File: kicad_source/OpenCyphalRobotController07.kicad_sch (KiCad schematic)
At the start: 23 parts, among them J1 SM04B-SRSS-TB, J2 RASPBERRYPI_PICO, J3 SM04B-SRSS-TB, J4 S3B-PH-SM4-TB, SW1 PTS636 SM43 SMTR LFS, U1 24LC64-I/SN

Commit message: made first draft of layout
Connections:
- net INH12: now also J2.15 (GP11/SPI1_TX/I2C1_SCL); no longer J2.14 (GP10/SPI1_SCK/I2C1_SDA)
- net INH34: now also J2.14 (GP10/SPI1_SCK/I2C1_SDA); no longer J2.15 (GP11/SPI1_TX/I2C1_SCL)
- net PWM1: now also J2.12 (GP9/SPI1_CS/I2C0_SCL/UART1_RX); no longer J2.9 (GP6/SPI0_SCK/I2C1_SDA)
- net PWM2: now also J2.11 (GP8/SPI1_RX/I2C0_SDA/UART1_TX); no longer J2.10 (GP7/SPI0_TX/I2C1_SCL)
- net PWM3: now also J2.10 (GP7/SPI0_TX/I2C1_SCL); no longer J2.11 (GP8/SPI1_RX/I2C0_SDA/UART1_TX)
- net PWM4: now also J2.9 (GP6/SPI0_SCK/I2C1_SDA); no longer J2.12 (GP9/SPI1_CS/I2C0_SCL/UART1_RX)
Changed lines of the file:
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@@
     (effects (font (size 1.27 1.27)) (justify right bottom))
   )
-  (label "PWM3" (at 53.34 57.15 180)
+  (label "PWM3" (at 53.34 54.61 180)
     (effects (font (size 1.27 1.27)) (justify right bottom))
   )
-  (label "PWM1" (at 53.34 52.07 180)
+  (label "PWM1" (at 53.34 59.69 180)
     (effects (font (size 1.27 1.27)) (justify right bottom))
   )
@@
     (effects (font (size 1.27 1.27)) (justify right bottom))
   )
-  (label "INH34" (at 53.34 67.31 180)
+  (label "INH34" (at 53.34 64.77 180)
     (effects (font (size 1.27 1.27)) (justify right bottom))
   )
@@
     (effects (font (size 1.27 1.27)) (justify left bottom))
   )
-  (label "INH12" (at 53.34 64.77 180)
+  (label "INH12" (at 53.34 67.31 180)
     (effects (font (size 1.27 1.27)) (justify right bottom))
   )
-  (label "PWM2" (at 53.34 54.61 180)
+  (label "PWM2" (at 53.34 57.15 180)
     (effects (font (size 1.27 1.27)) (justify right bottom))
   )
@@
     (effects (font (size 1.27 1.27)) (justify left bottom))
   )
-  (label "PWM4" (at 53.34 59.69 180)
+  (label "PWM4" (at 53.34 52.07 180)
     (effects (font (size 1.27 1.27)) (justify right bottom))
   )
@@
     (effects (font (size 1.27 1.27)) (justify right bottom))
   )
-  (global_label "PWM1" (shape output) (at 40.64 52.07 180) (fields_autoplaced)
+  (global_label "PWM1" (shape output) (at 40.64 59.69 180) (fields_autoplaced)
     (effects (font (size 1.27 1.27)) (justify right))
-    (property "Referenzen zwischen Schaltplänen" "${INTERSHEET_REFS}" (id 0) (at 32.9334 51.9906 0)
+    (property "Referenzen zwischen Schaltplänen" "${INTERSHEET_REFS}" (id 0) (at 32.9334 59.6106 0)
       (effects (font (size 1.27 1.27)) (justify right) hide)
     )
@@
     )
   )
-  (global_label "PWM2" (shape output) (at 40.64 54.61 180) (fields_autoplaced)
+  (global_label "PWM2" (shape output) (at 40.64 57.15 180) (fields_autoplaced)
+    (effects (font (size 1.27 1.27)) (justify right))
+    (property "Referenzen zwischen Schaltplänen" "${INTERSHEET_REFS}" (id 0) (at 32.9334 57.0706 0)
+      (effects (font (size 1.27 1.27)) (justify right) hide)
+    )
+  )
+  (global_label "PWM3" (shape output) (at 40.64 54.61 180) (fields_autoplaced)
     (effects (font (size 1.27 1.27)) (justify right))
     (property "Referenzen zwischen Schaltplänen" "${INTERSHEET_REFS}" (id 0) (at 32.9334 54.5306 0)
@@
     )
   )
-  (global_label "PWM3" (shape output) (at 40.64 57.15 180) (fields_autoplaced)
+  (global_label "INH12" (shape output) (at 40.64 67.31 180) (fields_autoplaced)
     (effects (font (size 1.27 1.27)) (justify right))
-    (property "Referenzen zwischen Schaltplänen" "${INTERSHEET_REFS}" (id 0) (at 32.9334 57.0706 0)
-      (effects (font (size 1.27 1.27)) (justify right) hide)
-    )
-  )
-  (global_label "INH12" (shape output) (at 40.64 64.77 180) (fields_autoplaced)
-    (effects (font (size 1.27 1.27)) (justify right))
-    (property "Referenzen zwischen Schaltplänen" "${INTERSHEET_REFS}" (id 0) (at 32.631 64.6906 0)
+    (property "Referenzen zwischen Schaltplänen" "${INTERSHEET_REFS}" (id 0) (at 32.631 67.2306 0)
       (effects (font (size 1.27 1.27)) (justify right) hide)
     )
@@
     )
   )
-  (global_label "INH34" (shape output) (at 40.64 67.31 180) (fields_autoplaced)
+  (global_label "INH34" (shape output) (at 40.64 64.77 180) (fields_autoplaced)
     (effects (font (size 1.27 1.27)) (justify right))
-    (property "Referenzen zwischen Schaltplänen" "${INTERSHEET_REFS}" (id 0) (at 32.631 67.2306 0)
+    (property "Referenzen zwischen Schaltplänen" "${INTERSHEET_REFS}" (id 0) (at 32.631 64.6906 0)
       (effects (font (size 1.27 1.27)) (justify right) hide)
     )
   )
-  (global_label "PWM4" (shape output) (at 40.64 59.69 180) (fields_autoplaced)
+  (global_label "PWM4" (shape output) (at 40.64 52.07 180) (fields_autoplaced)
     (effects (font (size 1.27 1.27)) (justify right))
-    (property "Referenzen zwischen Schaltplänen" "${INTERSHEET_REFS}" (id 0) (at 32.9334 59.6106 0)
+    (property "Referenzen zwischen Schaltplänen" "${INTERSHEET_REFS}" (id 0) (at 32.9334 51.9906 0)
       (effects (font (size 1.27 1.27)) (justify right) hide)
     )
@@
     )
     (path "/00000000-0000-0000-0000-00005ed92f9c/00000000-0000-0000-0000-000062500ca8"
-      (reference "J5") (unit 1) (value "SM04B-GHS-TB") (footprint "Connector_JST:JST_GH_SM04B-GHS-TB_1x04-1MP_P1.25mm_Horizontal")
+      (reference "J5") (unit 1) (value "BM04B-GHS-TBT") (footprint "Connector_JST:JST_GH_BM04B-GHS-TBT_1x04-1MP_P1.25mm_Vertical")
     )
     (path "/00000000-0000-0000-0000-00005ed92f9c/00000000-0000-0000-0000-000062500cbc"
-      (reference "J6") (unit 1) (value "SM04B-GHS-TB") (footprint "Connector_JST:JST_GH_SM04B-GHS-TB_1x04-1MP_P1.25mm_Horizontal")
+      (reference "J6") (unit 1) (value "BM04B-GHS-TBT") (footprint "Connector_JST:JST_GH_BM04B-GHS-TBT_1x04-1MP_P1.25mm_Vertical")
     )
     (path "/29c3546c-5738-4410-83a1-968e85712add/00000000-0000-0000-0000-00005dfcab9e"

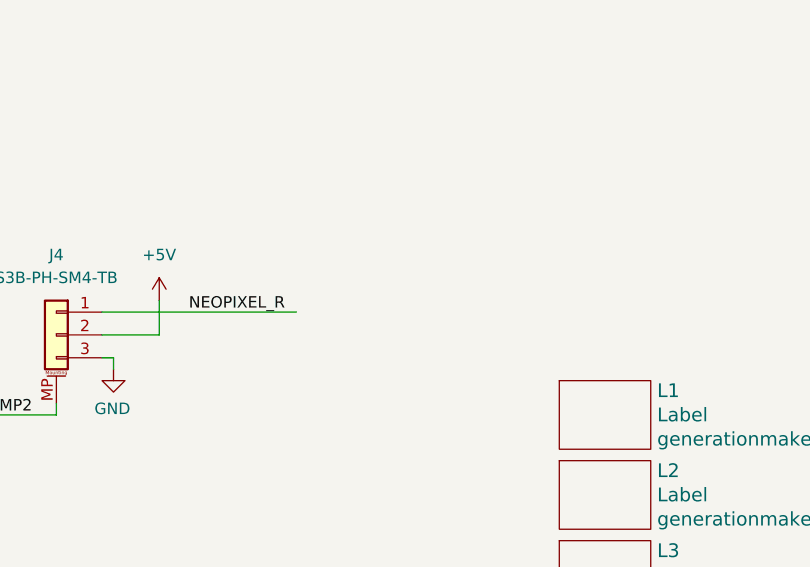
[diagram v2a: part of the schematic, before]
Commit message: reworked shape of PCB to fit into T07, added hole for USB connector
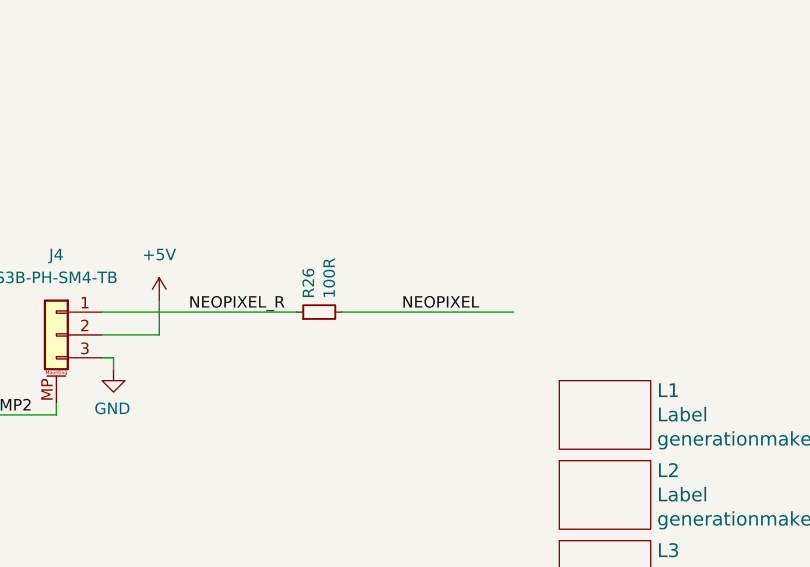
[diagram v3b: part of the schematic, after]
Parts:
- added R26: 100R, Resistor_SMD:R_0603_1608Metric, symbol Device:R_Small
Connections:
- net NEOPIXEL: now also R26.2
- net NEOPIXEL_R: now also R26.1
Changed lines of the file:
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@@
+    (stroke (width 0) (type default) (color 0 0 0 0))
+  )
+  (wire (pts (xy 194.31 130.81) (xy 213.36 130.81))
     (stroke (width 0) (type default) (color 0 0 0 0))
   )
@@
   (label "SER_TX" (at 45.72 31.75 0)
     (effects (font (size 1.27 1.27)) (justify left bottom))
+  )
+  (label "NEOPIXEL" (at 209.55 130.81 180)
+    (effects (font (size 1.27 1.27)) (justify right bottom))
   )
   (label "MP2" (at 55.88 181.61 0)
@@
     (pin "1")
   )
+  (symbol (lib_id "Device:R_Small") (at 191.77 130.81 90) (unit 1)
+    (in_bom yes) (on_board yes)
+    (property "Reference" "R26" (id 0) (at 190.6016 129.3114 0)
+      (effects (font (size 1.27 1.27)) (justify left))
+    )
+    (property "Value" "100R" (id 1) (at 192.913 129.3114 0)
+      (effects (font (size 1.27 1.27)) (justify left))
+    )
+    (property "Footprint" "Resistor_SMD:R_0603_1608Metric" (id 2) (at 195.58 130.81 0)
+      (effects (font (size 1.27 1.27)) hide)
+    )
+    (property "Datasheet" "~" (id 3) (at 191.77 130.81 0))
+    (pin "1")
+    (pin "2")
+  )
   (symbol (lib_id "Connector_Generic_MountingPin:Conn_01x03_MountingPin") (at 162.56 133.35 0) (mirror y) (unit 1)
     (in_bom yes) (on_board yes) (fields_autoplaced)
@@
       (reference "R25") (unit 1) (value "10k") (footprint "Resistor_SMD:R_0603_1608Metric")
     )
+    (path "/06b11e0e-c73c-4dc6-8276-21bc43869015"
+      (reference "R26") (unit 1) (value "100R") (footprint "Resistor_SMD:R_0603_1608Metric")
+    )
     (path "/f22e738d-7eb9-478a-98ea-a8bc262180f6/00000000-0000-0000-0000-00005dea6cab"

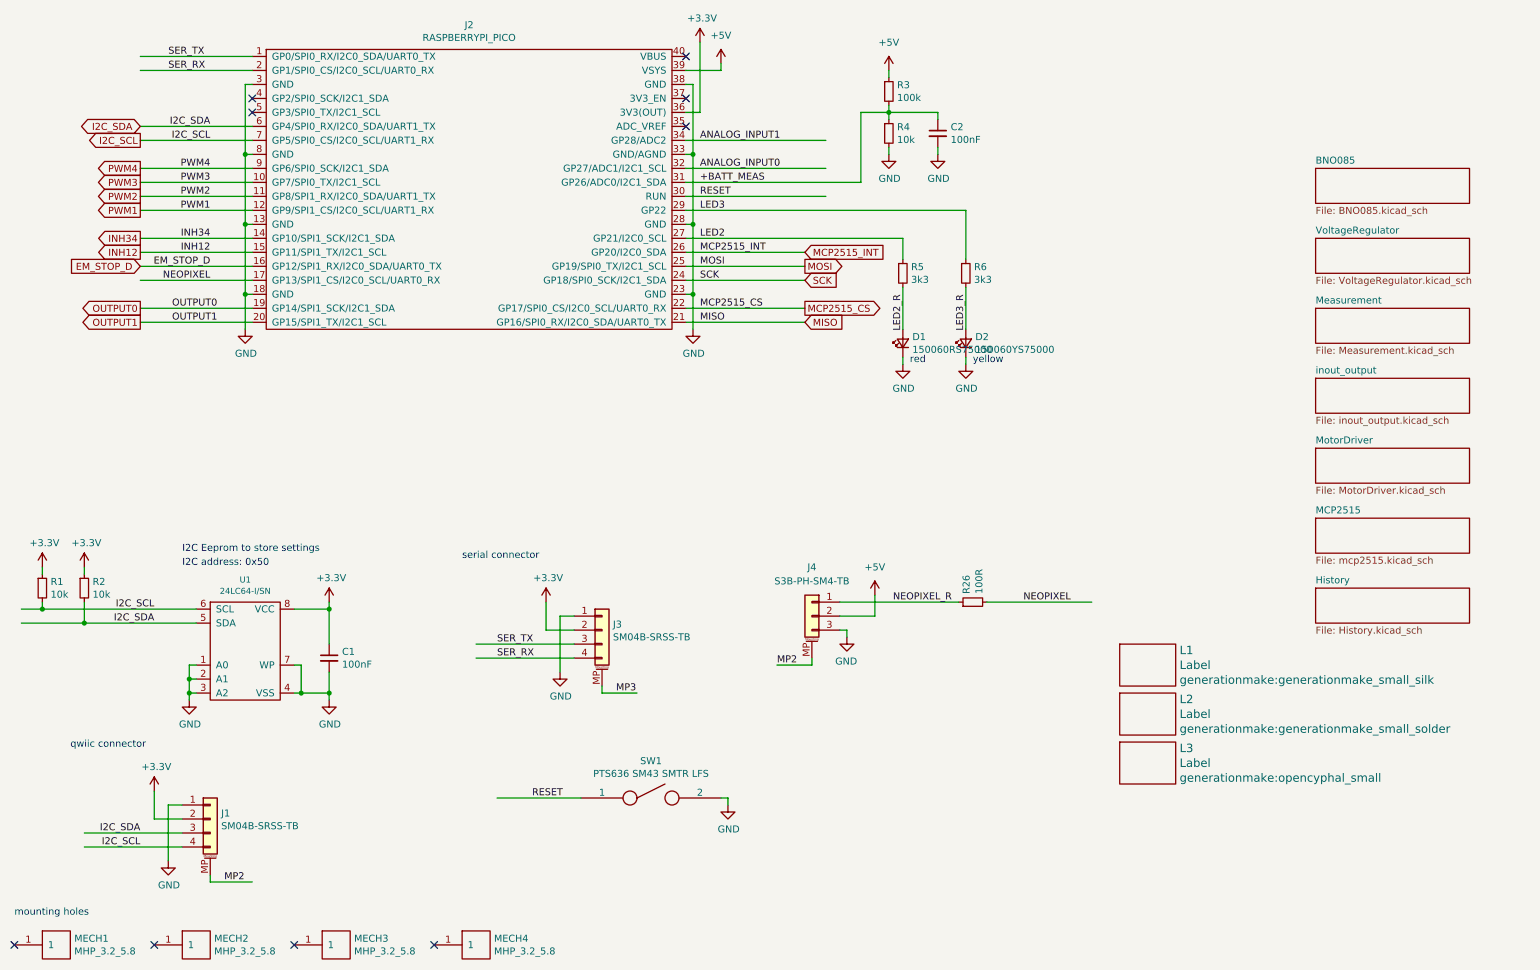
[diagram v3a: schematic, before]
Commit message: added connector for quad encoder
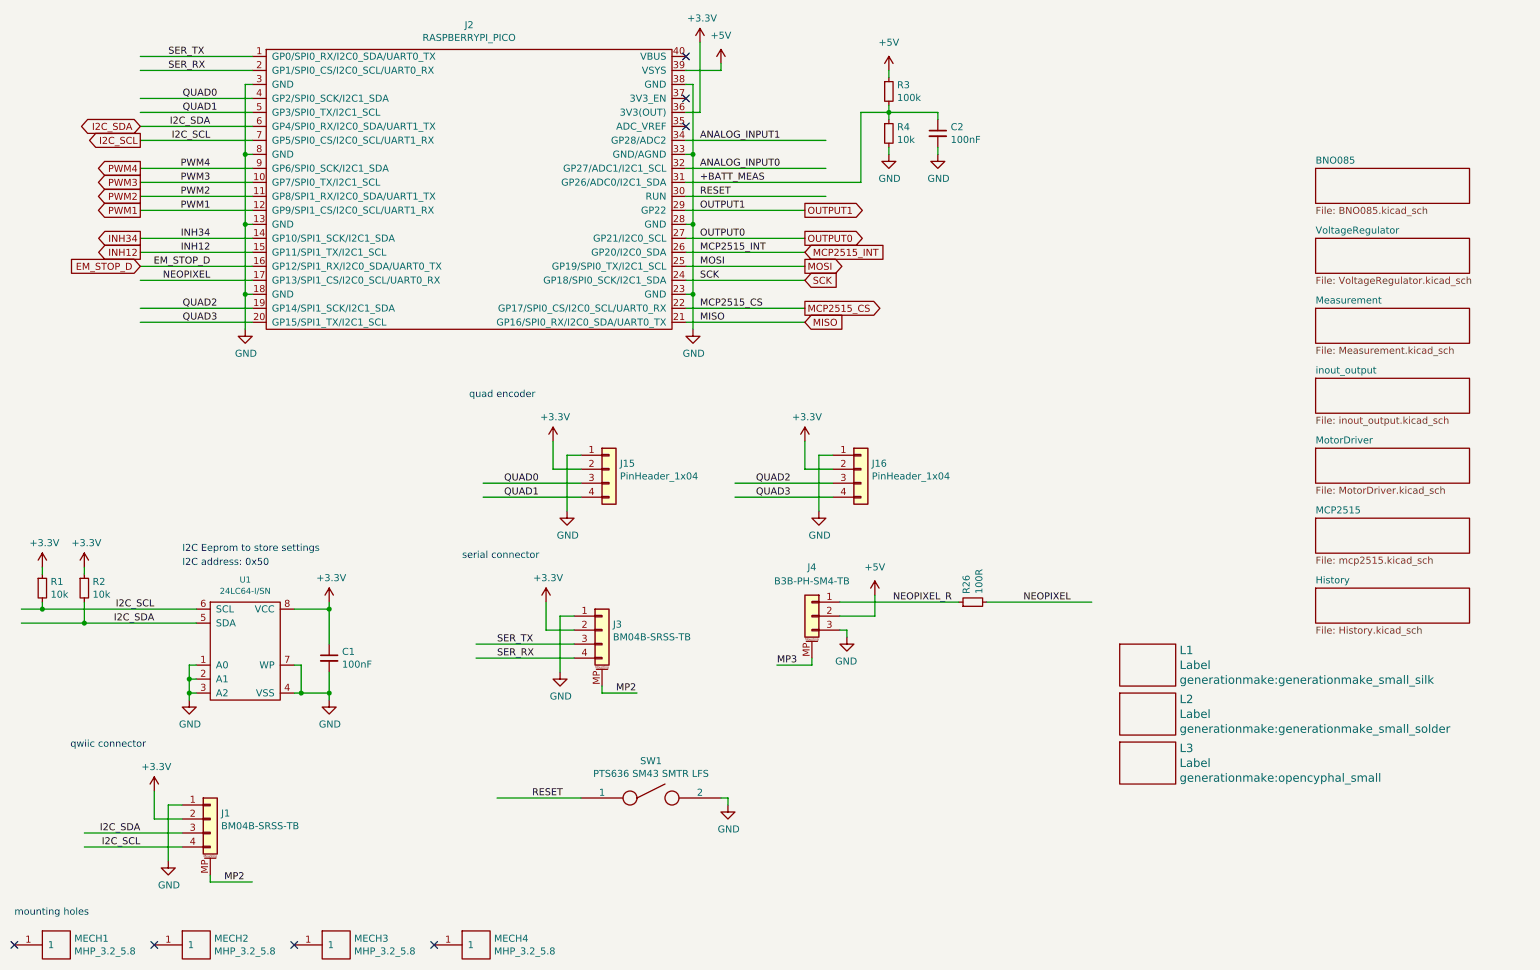
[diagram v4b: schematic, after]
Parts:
- removed D1: 150060RS75000, LED_SMD:LED_0603_1608Metric, symbol Device:LED_Small
- removed D2: 150060YS75000, LED_SMD:LED_0603_1608Metric, symbol Device:LED_Small
- removed R5, R6: 3k3, Resistor_SMD:R_0603_1608Metric, symbol Device:R_Small
- added J15, J16: PinHeader_1x04, Connector_PinHeader_2.54mm:PinHeader_1x04_P2.54mm_Vertical, symbol Connector_Generic:Conn_01x04
- J1, J3: value SM04B-SRSS-TB -> BM04B-SRSS-TB; footprint Connector_JST:JST_SH_SM04B-SRSS-TB_1x04-1MP_P1.00mm_Horizontal -> Connector_JST:JST_SH_BM04B-SRSS-TB_1x04-1MP_P1.00mm_Vertical
- J4: value S3B-PH-SM4-TB -> B3B-PH-SM4-TB; footprint Connector_JST:JST_PH_S3B-PH-SM4-TB_1x03-1MP_P2.00mm_Horizontal -> Connector_JST:JST_PH_B3B-PH-SM4-TB_1x03-1MP_P2.00mm_Vertical
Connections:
- net LED2 is gone; now on net OUTPUT0: J2.27 (GP21/I2C0_SCL)
- net LED3 is gone; now on net OUTPUT1: J2.29 (GP22)
- net +3.3V: now also J15.2 (Pin_2), J16.2 (Pin_2)
- net GND: now also J15.1 (Pin_1), J16.1 (Pin_1)
- net MP2: now also J3.MP (MountPin); no longer J4.MP (MountPin)
- net MP3: now also J4.MP (MountPin); no longer J3.MP (MountPin)
- net OUTPUT0: no longer J2.19 (GP14/SPI1_SCK/I2C1_SDA)
- net OUTPUT1: no longer J2.20 (GP15/SPI1_TX/I2C1_SCL)
- net QUAD0: now reaches J2.4 (GP2/SPI0_SCK/I2C1_SDA)
- net QUAD0: now also J15.3 (Pin_3)
- net QUAD1: now reaches J2.5 (GP3/SPI0_TX/I2C1_SCL)
- net QUAD1: now also J15.4 (Pin_4)
- new net QUAD2: J16.3 (Pin_3), J2.19 (GP14/SPI1_SCK/I2C1_SDA)
- new net QUAD3: J16.4 (Pin_4), J2.20 (GP15/SPI1_TX/I2C1_SCL)
- no-connect marks 9 -> 7
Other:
- note added: "quad encoder"
- note removed: "red"
- note removed: "yellow"

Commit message: finished layout
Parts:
- removed C2: 100nF, Capacitor_SMD:C_0603_1608Metric, symbol Device:C_Small
- removed R3: 100k, Resistor_SMD:R_0603_1608Metric, symbol Device:R_Small
- removed R4: 10k, Resistor_SMD:R_0603_1608Metric, symbol Device:R_Small
- added J17: PinHeader_1x05, Connector_PinHeader_2.54mm:PinHeader_1x05_P2.54mm_Vertical, symbol Connector_Generic:Conn_01x05
- J2: footprint generationmake:RASPI_PICO_SOLDER_ONLY -> generationmake:RASPI_PICO_SOLDER_Kopie
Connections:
- net +BATT_MEAS is gone; now on net ANALOG_INPUT0: J2.31 (GP26/ADC0/I2C1_SDA)
- net +3.3V: now also J17.2 (Pin_2)
- net ANALOG_INPUT0: now also J17.5 (Pin_5); no longer J2.32 (GP27/ADC1/I2C1_SCL)
- net ANALOG_INPUT1: now also J2.32 (GP27/ADC1/I2C1_SCL), J17.4 (Pin_4); no longer J2.34 (GP28/ADC2)
- net GND: now also J17.1 (Pin_1)
- new net ANALOG_INPUT2: J17.3 (Pin_3), J2.34 (GP28/ADC2)
